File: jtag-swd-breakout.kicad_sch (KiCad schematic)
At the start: 3 parts, among them J1 JTAG, J3 68000-103HLF, J6 DS1021-1*6SF11-B

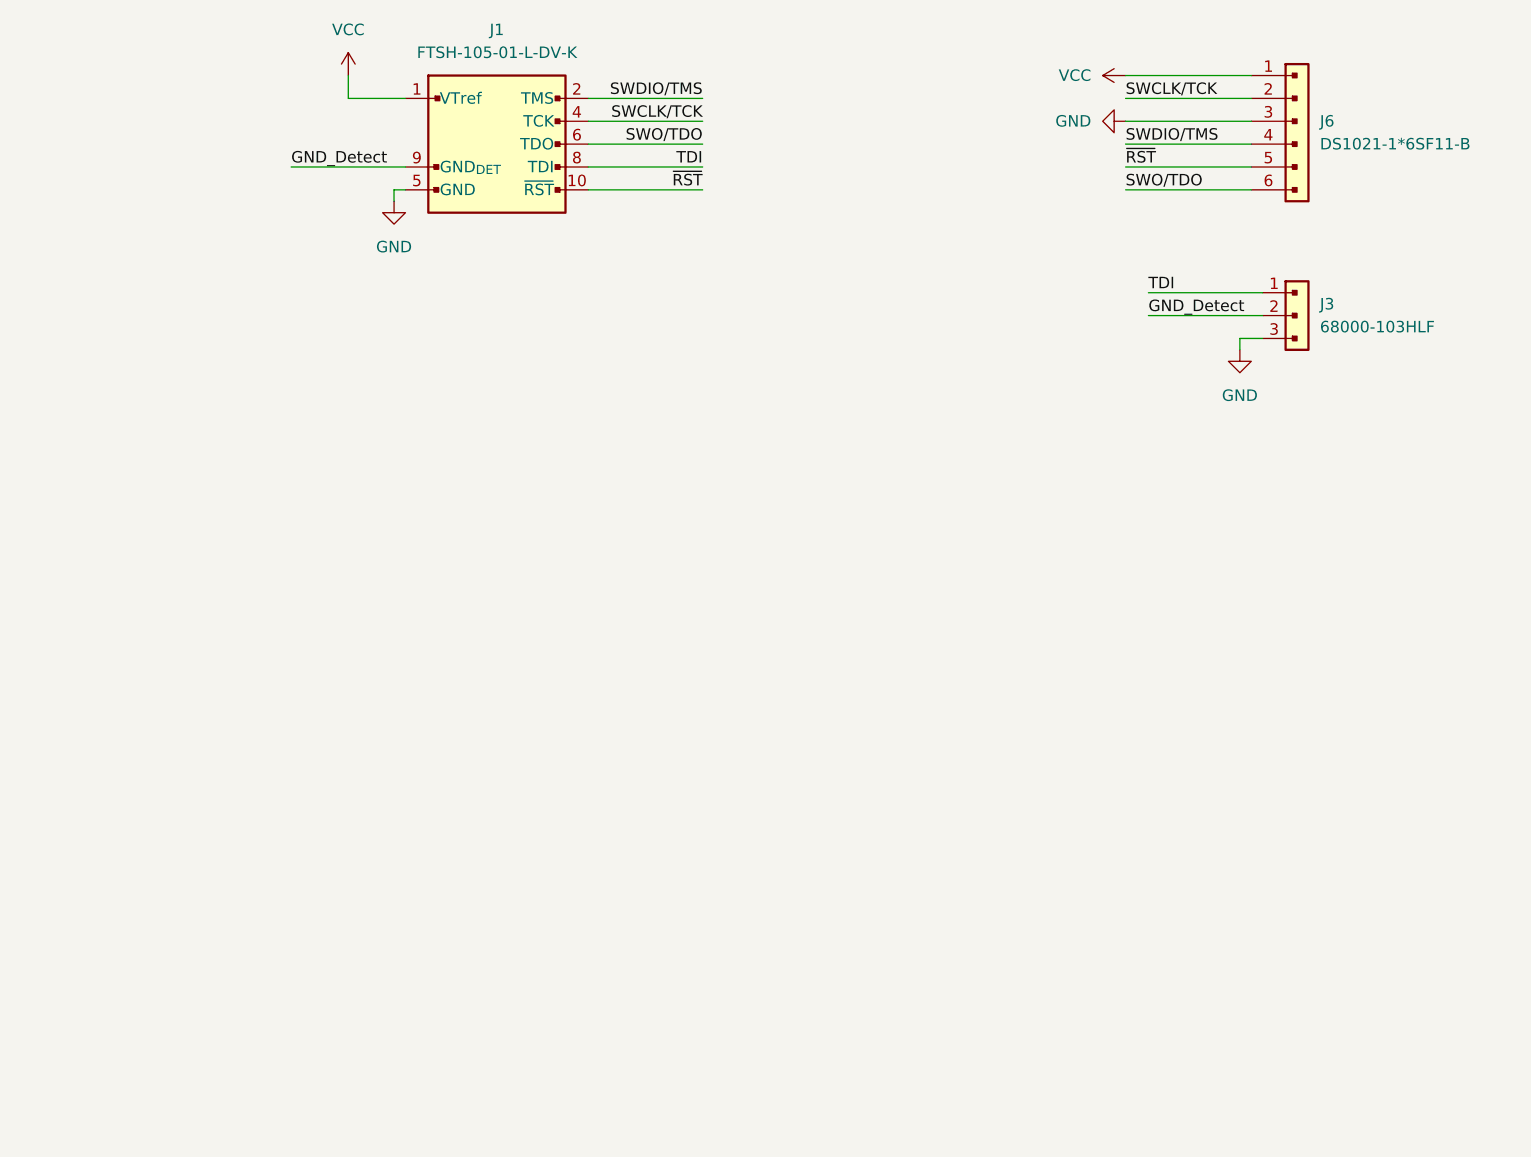
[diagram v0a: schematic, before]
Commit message: Add JTAG 20
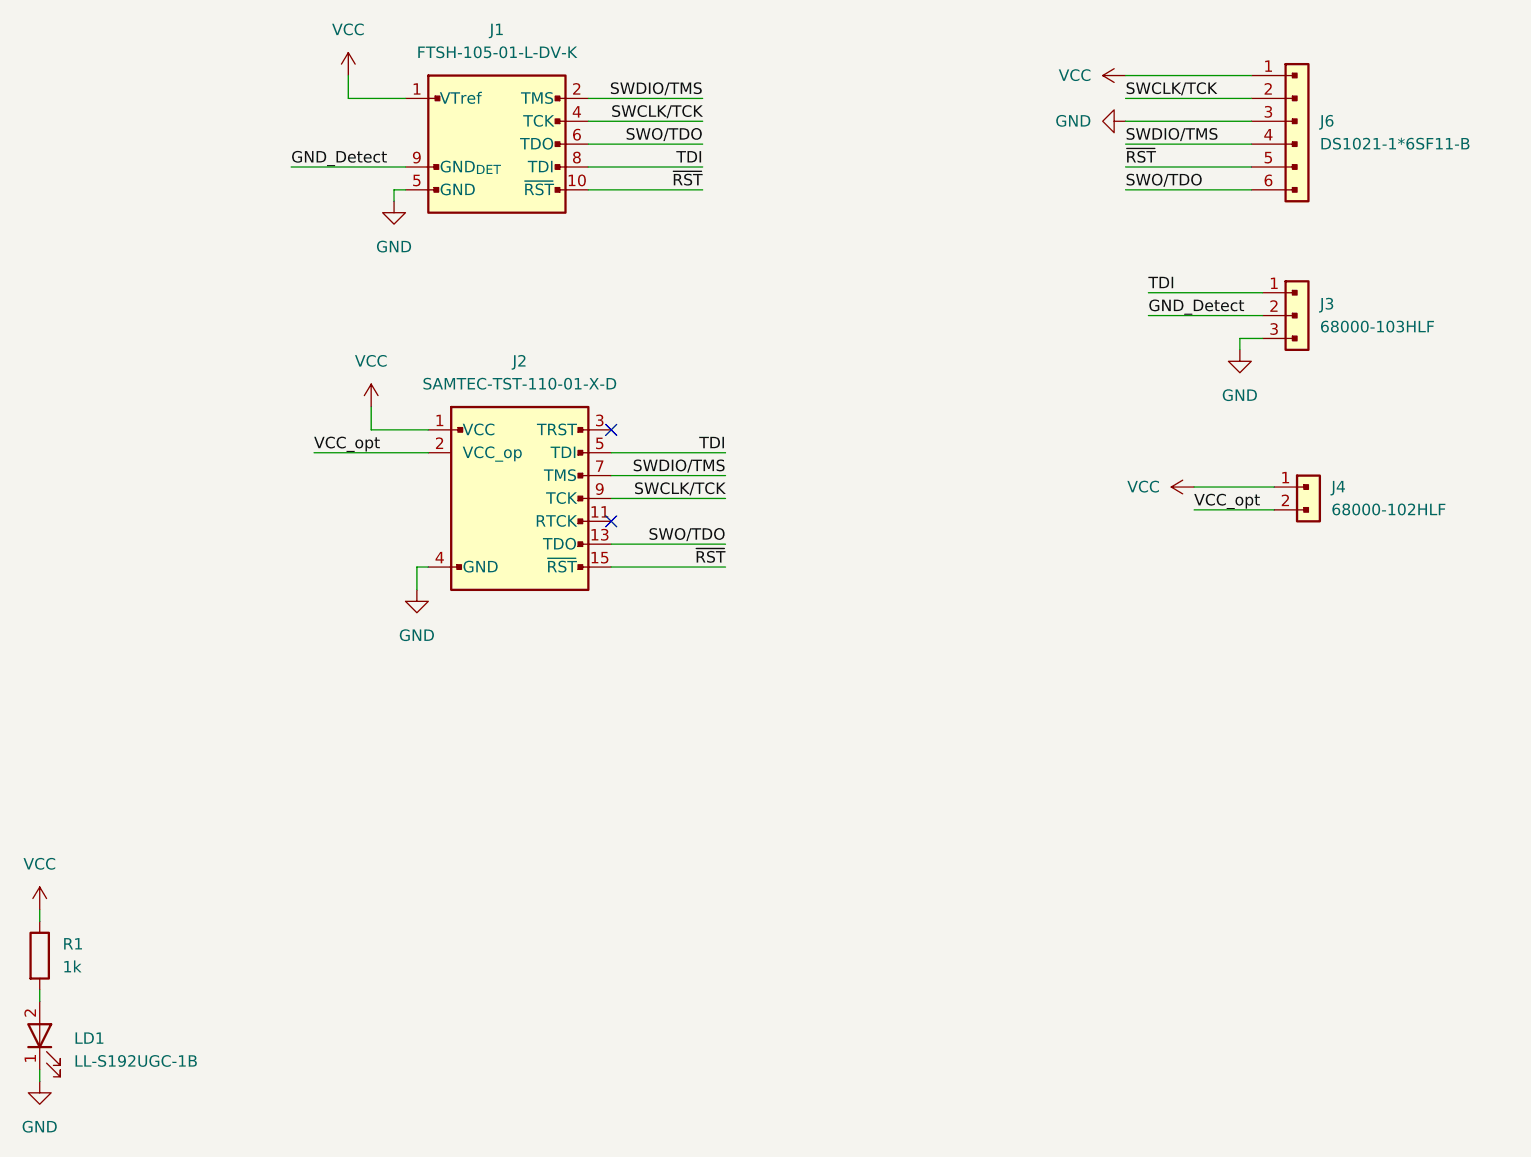
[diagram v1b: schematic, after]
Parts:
- added J2: ~, Koszalix_Connectors_PinHead:SAMTEC-TST-110-01-X-D, symbol Koszalix_Connectors_PinHead:Connector_JTAG_20
- added J4: 68000-102HLF, Koszalix_Connectors_PinHead:Amphenol_68000_102HLF, symbol Koszalix_Connectors_PinHead:PinHeader_1x2
- added LD1: LL-S192UGC-1B, LED_SMD:LED_0603_1608Metric, symbol Koszalix_LED:LL-S192UGC-1B
- added R1: 1k, Resistor_SMD:R_0603_1608Metric, symbol Koszalix_Resistors_Yageo_RC0603:RES_1k_0603
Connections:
- net GND: now also J2.10 (GND), J2.12 (GND), J2.14 (GND), J2.16 (GND), J2.18 (GND), J2.20 (GND), J2.4 (GND), J2.6 (GND), J2.8 (GND), LD1.1
- net SWCLK/TCK: now also J2.9 (TCK)
- net SWDIO/TMS: now also J2.7 (TMS)
- net SWO/TDO: now also J2.13 (TDO)
- net TDI: now also J2.5 (TDI)
- net VCC: now also J2.1 (VCC), J4.1, R1.1
- net ~{RST}: now also J2.15 (~{RST})
- new net: LD1.2, R1.2
- new net VCC_opt: J2.2 (VCC_op), J4.2
- no-connect marks 0 -> 2

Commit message: Update adapter
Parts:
- removed J3: 68000-103HLF, Koszalix_Connectors_PinHead:Amphenol_68000-103HLF, symbol Koszalix_Connectors_PinHead:PinHeader_1x3
- added J3: DS1021-1*4SF11-B, Connector_PinHeader_2.54mm:PinHeader_1x04_P2.54mm_Vertical, symbol Koszalix_Connectors_PinHead:PinHeader_1x4
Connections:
- net GND_Detect: now also J3.1 (Pin_1)
- net TDI: now also J3.2 (Pin_2)
- net RTCK: now reaches J2.11 (RTCK)
- net RTCK: now also J3.4 (Pin_4)
- net TRST: now reaches J2.3 (TRST)
- net TRST: now also J3.3 (Pin_3)
- no-connect marks 2 -> 0
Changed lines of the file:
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@@
 		(rev "1.0.0")
 	)
-	(no_connect
-		(at 87.63 107.95)
-	)
-	(no_connect
-		(at 87.63 118.11)
-	)
 	(wire
 		(pts
@@
 	(wire
 		(pts
+			(xy 87.63 107.95) (xy 100.33 107.95)
+		)
+		(stroke
+			(width 0)
+			(type default)
+		)
+	)
+	(wire
+		(pts
 			(xy 152.4 116.84) (xy 161.29 116.84)
 		)
@@
 	(wire
 		(pts
+			(xy 142.24 151.13) (xy 154.94 151.13)
+		)
+		(stroke
+			(width 0)
+			(type default)
+		)
+	)
+	(wire
+		(pts
+			(xy 142.24 146.05) (xy 154.94 146.05)
+		)
+		(stroke
+			(width 0)
+			(type default)
+		)
+	)
+	(wire
+		(pts
 			(xy 144.78 81.28) (xy 158.75 81.28)
 		)
@@
 	(wire
 		(pts
-			(xy 147.32 92.71) (xy 160.02 92.71)
-		)
-		(stroke
-			(width 0)
-			(type default)
-		)
-	)
-	(wire
-		(pts
-			(xy 147.32 95.25) (xy 160.02 95.25)
-		)
-		(stroke
-			(width 0)
-			(type default)
-		)
-	)
-	(wire
-		(pts
-			(xy 157.48 97.79) (xy 160.02 97.79)
-		)
-		(stroke
-			(width 0)
-			(type default)
-		)
-	)
-	(wire
-		(pts
 			(xy 100.33 110.49) (xy 87.63 110.49)
 		)
@@
 	(wire
 		(pts
-			(xy 157.48 99.06) (xy 157.48 97.79)
+			(xy 142.24 148.59) (xy 154.94 148.59)
 		)
 		(stroke
@@
 	(wire
 		(pts
+			(xy 142.24 153.67) (xy 154.94 153.67)
+		)
+		(stroke
+			(width 0)
+			(type default)
+		)
+	)
+	(wire
+		(pts
 			(xy 24.13 162.56) (xy 24.13 161.29)
 		)
@@
 		(pts
 			(xy 58.42 68.58) (xy 58.42 71.12)
+		)
+		(stroke
+			(width 0)
+			(type default)
+		)
+	)
+	(wire
+		(pts
+			(xy 87.63 118.11) (xy 100.33 118.11)
 		)
 		(stroke
@@
 	)
 	(label "GND_Detect"
-		(at 147.32 95.25 0)
+		(at 142.24 146.05 0)
 		(fields_autoplaced yes)
 		(effects
@@
 	)
 	(label "TDI"
-		(at 147.32 92.71 0)
+		(at 142.24 148.59 0)
 		(fields_autoplaced yes)
 		(effects
@@
 			)
 			(justify left bottom)
+		)
+	)
+	(label "TRST"
+		(at 100.33 107.95 180)
+		(fields_autoplaced yes)
+		(effects
+			(font
+				(size 1.27 1.27)
+			)
+			(justify right bottom)
+		)
+	)
+	(label "TRST"
+		(at 142.24 151.13 0)
+		(fields_autoplaced yes)
+		(effects
+			(font
+				(size 1.27 1.27)
+			)
+			(justify left bottom)
+		)
+	)
+	(label "RTCK"
+		(at 100.33 118.11 180)
+		(fields_autoplaced yes)
+		(effects
+			(font
+				(size 1.27 1.27)
+			)
+			(justify right bottom)
 		)
 	)
@@
 			)
 			(justify right bottom)
+		)
+	)
+	(label "RTCK"
+		(at 142.24 153.67 0)
+		(fields_autoplaced yes)
+		(effects
+			(font
+				(size 1.27 1.27)
+			)
+			(justify left bottom)
 		)
 	)
@@
 	)
 	(symbol
-		(lib_id "Koszalix_Connectors_PinHead:PinHeader_1x3")
-		(at 160.02 92.71 0)
+		(lib_id "Koszalix_Connectors_PinHead:PinHeader_1x4")
+		(at 154.94 146.05 0)
 		(unit 1)
 		(exclude_from_sim no)
@@
 		(fields_autoplaced yes)
 		(property "Reference" "J3"
-			(at 166.37 93.9799 0)
+			(at 162.56 148.5899 0)
 			(effects
 				(font
@@
 			)
 		)
-		(property "Value" "68000-103HLF"
-			(at 167.64 96.52 0)
+		(property "Value" "DS1021-1*4SF11-B"
+			(at 155.448 141.986 0)
+			(effects
+				(font
+					(size 1.27 1.27)
+				)
+				(hide yes)
+			)
+		)
+		(property "Footprint" "Connector_PinHeader_2.54mm:PinHeader_1x04_P2.54mm_Vertical"
+			(at 155.448 141.986 0)
+			(effects
+				(font
+					(size 1.27 1.27)
+				)
+				(hide yes)
+			)
+		)
+		(property "Datasheet" "https://www.tme.eu/Document/cc301e58a5da78cb543a94b5a5b7f06a/DS1021.pdf"
+			(at 155.448 141.986 0)
+			(effects
+				(font
+					(size 1.27 1.27)
+				)
+				(hide yes)
+			)
+		)
+		(property "Description" "Pin Header connector 1x4"
+			(at 155.448 141.986 0)
+			(effects
+				(font
+					(size 1.27 1.27)
+				)
+				(hide yes)
+			)
+		)
+		(property "MPN" "DS1021-1*6SF11-B"
+			(at 162.56 151.1299 0)
+			(effects
+				(font
+					(size 1.27 1.27)
+				)
+				(justify left)
+			)
+		)
+		(property "Manufacturer" "Confly"
+			(at 150.368 143.002 0)
 			(effects
 				(font
@@
 			)
 		)
-		(property "Footprint" "Koszalix_Connectors_PinHead:Amphenol_68000-103HLF"
-			(at 167.64 99.06 0)
-			(effects
-				(font
-					(size 1.27 1.27)
-				)
-				(justify left bottom)
-				(hide yes)
-			)
-		)
-		(property "Datasheet" "https://www.tme.eu/Document/deb83b8ba474aa6382ee38bb24abad5e/68000-XXXXLF.pdf"
-			(at 167.64 101.6 0)
-			(effects
-				(font
-					(size 1.27 1.27)
-				)
-				(justify left bottom)
-				(hide yes)
-			)
-		)
-		(property "Description" "Pin Header connector 1x3"
-			(at 160.02 92.71 0)
-			(effects
-				(font
-					(size 1.27 1.27)
-				)
-				(hide yes)
-			)
-		)
-		(property "MPN" "68000-103HLF"
-			(at 166.37 96.5199 0)
-			(effects
-				(font
-					(size 1.27 1.27)
-				)
-				(justify left)
-			)
-		)
-		(property "Manufacuter" "Amphenol"
-			(at 167.64 106.68 0)
-			(effects
-				(font
-					(size 1.27 1.27)
-				)
-				(justify left bottom)
-				(hide yes)
-			)
+		(pin "1"
+		)
+		(pin "3"
+		)
+		(pin "4"
 		)
 		(pin "2"
-		)
-		(pin "3"
-		)
-		(pin "1"
 		)
 		(instances
@@
 					(unit 1)
 				)
-			)
-		)
-	)
-	(symbol
-		(lib_id "power:GND")
-		(at 157.48 99.06 0)
-		(unit 1)
-		(exclude_from_sim no)
-		(in_bom yes)
-		(on_board yes)
-		(dnp no)
-		(fields_autoplaced yes)
-		(property "Reference" "#PWR04"
-			(at 157.48 105.41 0)
-			(effects
-				(font
-					(size 1.27 1.27)
-				)
-				(hide yes)
-			)
-		)
-		(property "Value" "GND"
-			(at 157.48 104.14 0)
-			(effects
-				(font
-					(size 1.27 1.27)
-				)
-			)
-		)
-		(property "Footprint" ""
-			(at 157.48 99.06 0)
-			(effects
-				(font
-					(size 1.27 1.27)
-				)
-				(hide yes)
-			)
-		)
-		(property "Datasheet" ""
-			(at 157.48 99.06 0)
-			(effects
-				(font
-					(size 1.27 1.27)
-				)
-				(hide yes)
-			)
-		)
-		(property "Description" "Power symbol creates a global label with name \"GND\" , ground"
-			(at 157.48 99.06 0)
-			(effects
-				(font
-					(size 1.27 1.27)
-				)
-				(hide yes)
-			)
-		)
-		(pin "1"
-		)
-		(instances
-			(project "jtag-swd-breakout"
-				(path "/fedf2262-ccb8-4370-bef0-0057af82bdbf"
-					(reference "#PWR04")
-					(unit 1)
-				)
